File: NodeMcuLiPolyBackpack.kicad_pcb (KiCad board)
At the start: 2 copper layers, 13 parts, among them P1 switch, P2 5v G BAT, P3 CONN_01X02, U1 MCP73831

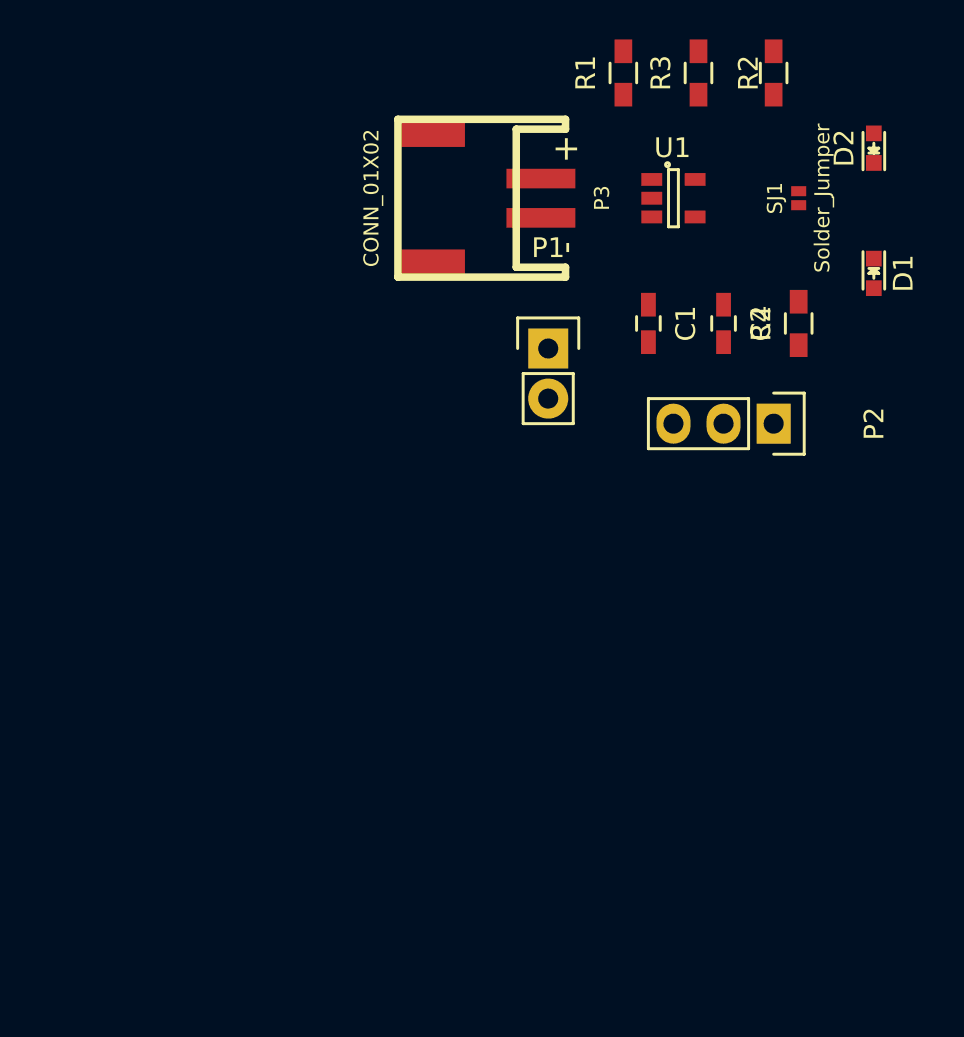
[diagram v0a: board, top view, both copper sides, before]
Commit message: Fix connector, add PCB
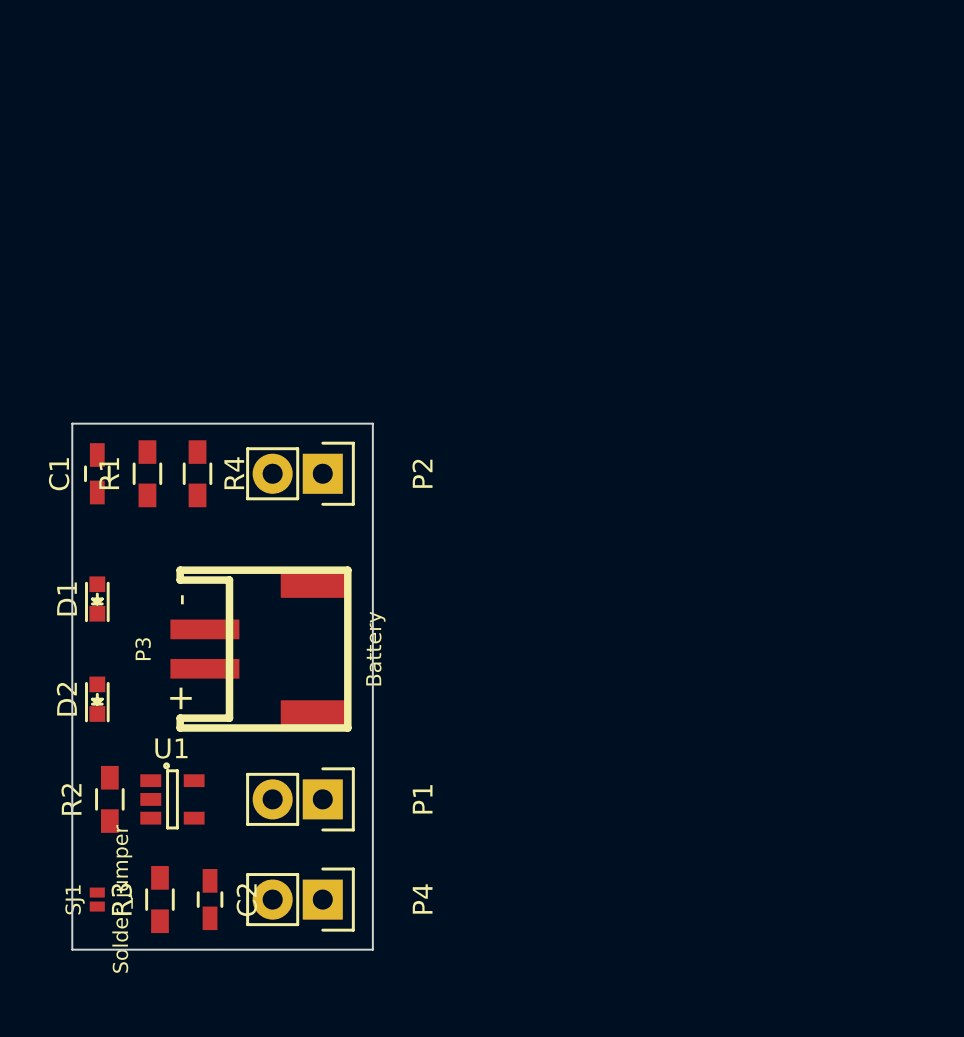
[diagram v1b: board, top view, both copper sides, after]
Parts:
- added P4: G 5V, Pin_Headers:Pin_Header_Straight_1x02, F.Cu at (139.7, 119.4)
- C1, C2: value C -> 10uF
- P1: value switch -> Switch
- P2: value 5v G BAT -> G BAT; footprint Pin_Headers:Pin_Header_Straight_1x03 -> Pin_Headers:Pin_Header_Straight_1x02
- P3: value CONN_01X02 -> Battery
- R1, R2: value R -> 1K
- R3: value R -> 10K
- R4: value R -> 2.5K
- SJ1: value Solder_Jumper -> Solder_jumper
- U1: footprint TO_SOT_Packages_SMD:SOT-23-5 -> Housings_SOT-23_SOT-143_TSOT-6:SOT-23-5
- moved SJ1 50.3 mm to (128.3, 119.4)
- moved R3 50.0 mm to (131.4, 119.4)
- moved R2 49.9 mm to (128.9, 114.3)
- moved D2 48.3 mm to (128.3, 109.2)
- moved D1 42.7 mm to (128.3, 104.1), turned to 90 degrees
- moved U1 39.7 mm to (132.1, 114.3)
- moved C2 39.1 mm to (134.0, 119.4)
- moved R1 31.5 mm to (130.8, 97.8)
- moved R4 31.4 mm to (133.3, 97.8), turned to 270 degrees
- moved C1 29.0 mm to (128.3, 97.8), turned to 90 degrees
- moved P1 25.6 mm to (139.7, 114.3), turned to 270 degrees
- moved P2 23.0 mm to (139.7, 97.8)
- moved P3 23.0 mm to (141.0, 106.7), turned to 90 degrees
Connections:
- R4 pad 2: Net-(R3-Pad2) -> Net-(R4-Pad2)
- SJ1 pad 1: Net-(SJ1-Pad1) -> Net-(R3-Pad2)
- SJ1 pad 2: GND -> Net-(R4-Pad2)
- U1 pad 2: Net-(SJ1-Pad1) -> GND
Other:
- board outline added: 15.2 x 26.7 mm
- rule pad_to_mask_clearance: 0.2 -> 0
